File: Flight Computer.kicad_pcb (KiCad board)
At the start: 4 copper layers, 27.5 x 83.3 mm, 90 parts, among them J1 Conn_01x08, J2 JTAG, Q1 DMP3099, Q2 2N7002, Q3 2N7002, Q4 2N7002, Q5 DMP3099, Q6 DMP3099, SW1 Reset, U1 VXO7803-1000, U2 W25Q16JVSS, U3 W25Q16JVSS, U4 Adafruit_GPS_THT, U5 ADXL345, U6 STM32F303RETx, U7 MAX7375AXR805, U8 BMP280

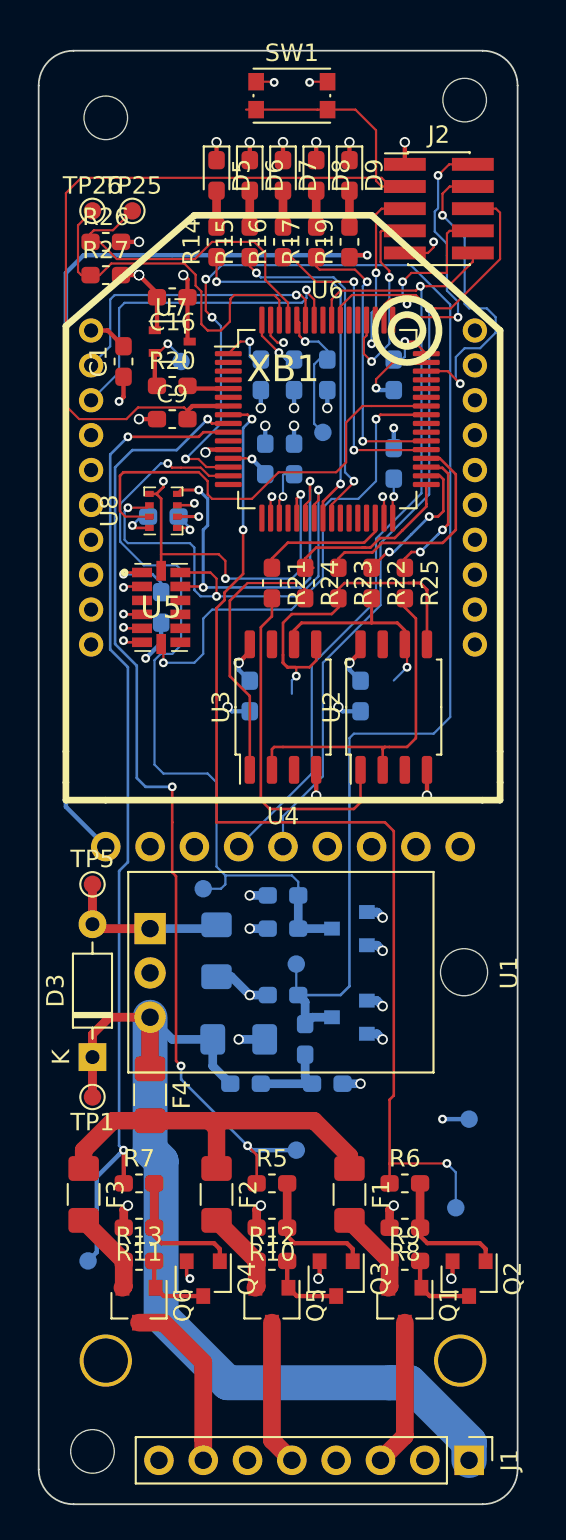
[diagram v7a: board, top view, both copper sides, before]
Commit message: Fixed silk Fixed JTAG Added PAYLOAD connector with I2C
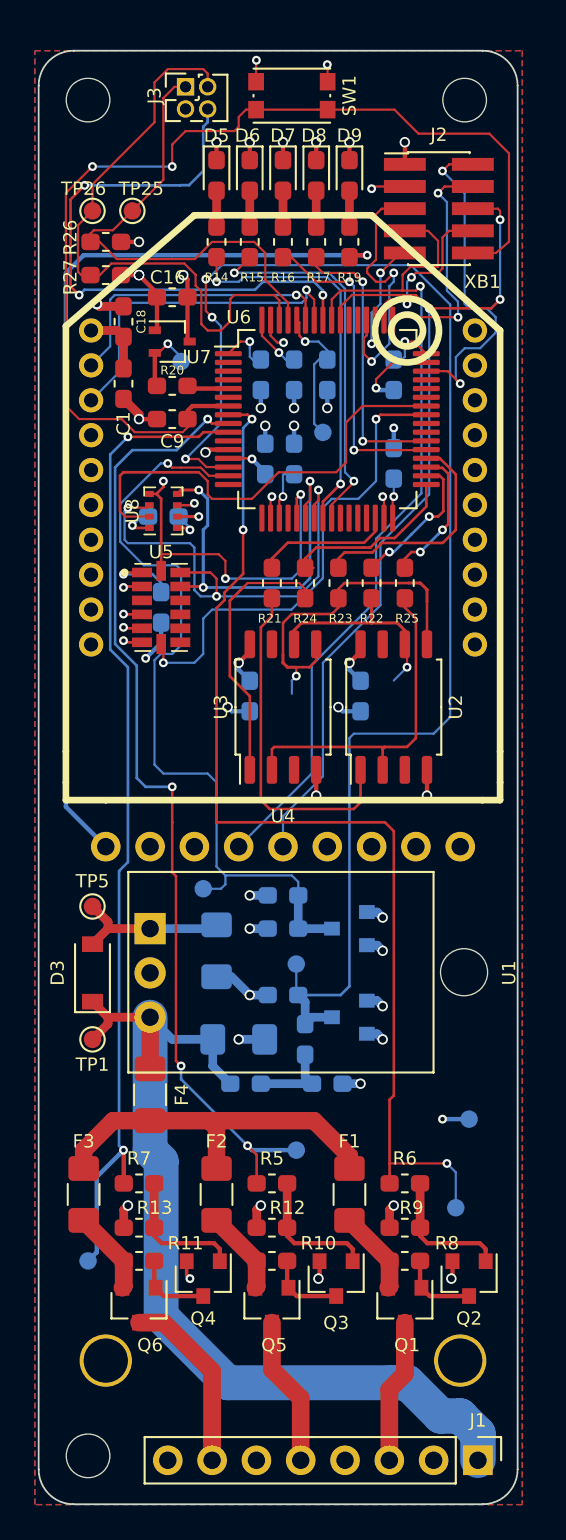
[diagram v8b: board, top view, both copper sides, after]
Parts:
- added C18: 47pF, Capacitor_SMD:C_0603_1608Metric_Pad1.05x0.95mm_HandSolder, F.Cu at (54.9, 65.5)
- added J3: PAYLOAD, Connector_PinHeader_1.27mm:PinHeader_2x02_P1.27mm_Vertical, F.Cu at (58.4, 52.1)
- C1: value 0.1uF -> 1uF
- D3: footprint Diode_THT:D_DO-35_SOD27_P7.62mm_Horizontal -> Diode_SMD:D_SOD-123
- moved G1 60.3 mm to (68.1, 52.1), turned to 180 degrees
- moved D3 4.83 mm to (53.1, 102.9)
- moved TP1 3.30 mm to (53.1, 106.7)
- moved H2 1.44 mm to (52.8, 52.8)
- moved C1 1.27 mm to (54.9, 69.1)
- moved TP5 1.27 mm to (53.1, 99.1)
- moved J1 0.51 mm to (75.2, 130.8)
- moved H3 0.36 mm to (52.8, 130.6)
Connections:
- J2 pad 10: /USART2_RX -> /MCU/NRST
- J2 pad 2: /MCU/SWDIO_JTCK -> /MCU/SWDIO_JTMS
- J2 pad 3: /MCU/NRST -> GND
- J2 pad 4: /MCU/SWDIO_JTMS -> /MCU/SWCLK_JTCK
- J2 pad 5: /MCU/USART3_TX -> /MCU/USART3_RX
- J2 pad 7: /MCU/USART3_RX -> /USART2_RX
- J2 pad 9: GND -> /MCU/USART3_TX
- U6 pad 49: /MCU/SWDIO_JTCK -> /MCU/SWCLK_JTCK
- U6 pad 57: (no net) -> /MCU/DEPLOY
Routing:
- net /MCU/DEPLOY: track 0.00 -> 33.8 mm, vias 0 -> 3
- net /MCU/SWDIO_JTCK: track 14.8 -> 0.00 mm, vias 2 -> 0
- net /MCU/SWCLK_JTCK: track 0.00 -> 13.6 mm, vias 0 -> 2
- net /MCU/I2C1_SCL: track 21.6 -> 34.7 mm
- net /MCU/I2C1_SDA: track 18.9 -> 27.6 mm
- net /MCU/NRST: track 55.4 -> 60.2 mm, vias 0 -> 2
- net /MCU/USART3_RX: track 12.1 -> 15.5 mm
- net /MCU/USART3_TX: track 10.8 -> 7.59 mm
- net /USART2_RX: track 47.2 -> 49.8 mm
- net GND: track 65.2 -> 67.6 mm
- net Net-(R15-Pad1): track 20.4 -> 21.9 mm
- net /USART2_TX: track 50.3 -> 51.8 mm, vias 1 -> 3
- net +3V3: track 52.6 -> 53.8 mm
- net +BATT: track 56.4 -> 55.2 mm
- net /MCU/SWDIO_JTMS: track 19.0 -> 19.8 mm
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- added copper zone on B.Cu, net GND
- added copper zone on F.Cu, net GND
